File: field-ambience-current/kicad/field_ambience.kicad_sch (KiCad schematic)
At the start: 0 parts

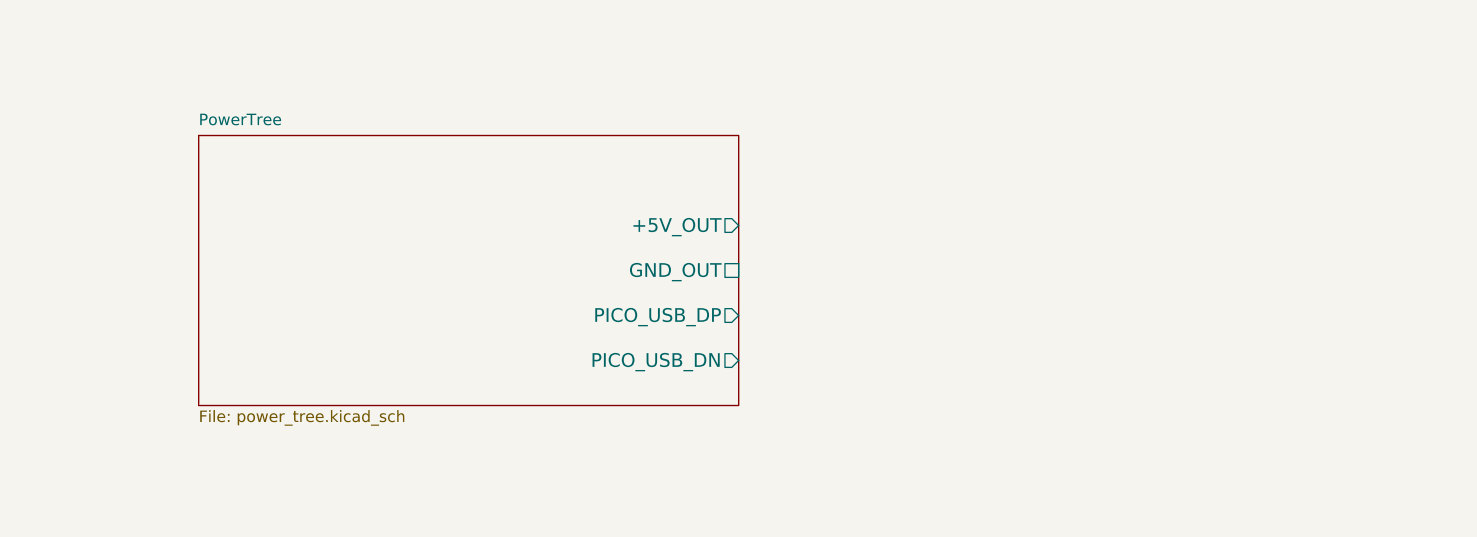
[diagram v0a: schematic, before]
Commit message: Add Sheet 2 (Pico 2) + fix Y-axis convention bug in Sheet 1
CRITICAL FIX in Sheet 1: lib_symbol pins use Y-UP (math) convention,
but schematic placement uses Y-DOWN (screen). Conversion is
abs_pin_y = sym_y - local_pin_y. The original Sheet 1 had USB-C
VBUS pins (A1/A4/B1/B4) actually wired to the GND trunk and GND
pins (A12/A9/B9/B12) wired to the +5V trunk — a power short if built.

Both sheets now use Y-DOWN coords throughout with explicit pin position
constants. The analyzer confirms correct pin_nets assignment:
- J1 (USB-C): VBUS pins → +5V_USB ✓, GND pins → GND ✓
- U1 (Pico 2): all 40 pins map to correct signals per SPEC v0.6 §5

Sheet 2 contents per SPEC v0.6 §5:
- U1 Raspberry Pi Pico 2 (40-pin module)
- All 22 functional GP pins routed to hierarchical outputs to Sheets 3-6
- C3 10µF + C4 100nF +3V3 decoupling near Pico pin 36
- SW11 Reset (6mm tactile) on RUN line with R_RUN pull-up
- SW12 BOOTSEL (DNP for THT-Pico variant)
- LED1 status LED with R19 820Ω current limit on GP26
- J4 3-pin SWD header (SWCLK/GND/SWDIO) for picoprobe debugging
- 8× GND power symbols on all Pico GND pins

Root sheet now contains both PowerTree + Pico sheets with inter-sheet
wires for +5V, USB_DP, USB_DN.

Analyzer status: 0 errors, 35 warnings (down from 39 before fix).
Remaining warnings are non-blocking: missing datasheets/ dir, NT-001
single-pin nets on hierarchical labels that will close in Sheets 3-7.
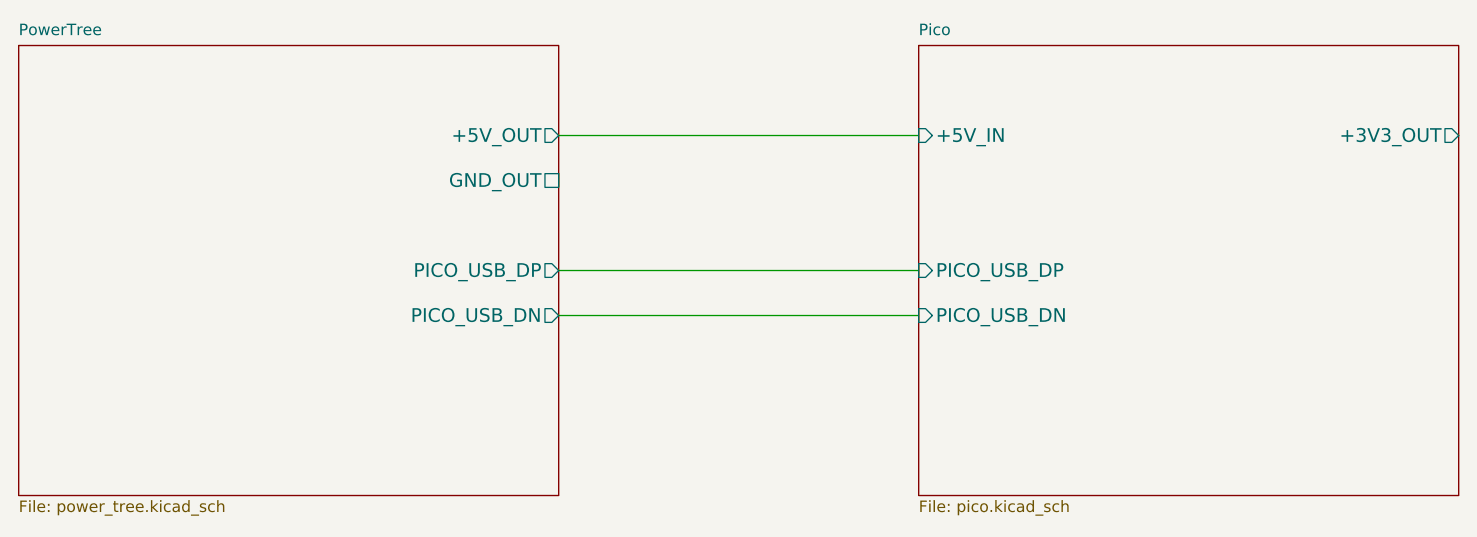
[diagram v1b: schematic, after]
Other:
- added sheet Pico (pico.kicad_sch)
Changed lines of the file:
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@@
     (rev "0.6")
     (company "Field Ambience Project"))
-  (sheet (at 50 50) (size 60 30) (fields_autoplaced)
+  (sheet (at 30 40) (size 60 50) (fields_autoplaced)
     (stroke (width 0.1524) (type solid))
     (fill (color 0 0 0 0.0000))
-    (property "Sheetname" "PowerTree" (at 50 49 0)
+    (property "Sheetname" "PowerTree" (at 30 39 0)
       (effects (font (size 1.27 1.27)) (justify left bottom)))
-    (property "Sheetfile" "power_tree.kicad_sch" (at 50 80.5 0)
+    (property "Sheetfile" "power_tree.kicad_sch" (at 30 90.5 0)
       (effects (font (size 1.27 1.27)) (justify left top)))
-    (pin "+5V_OUT" output (at 110 60 0)
+    (pin "+5V_OUT" output (at 90 50 0)
       (effects (font (size 1.524 1.524)) (justify right))
 )
-    (pin "GND_OUT" passive (at 110 65 0)
+    (pin "GND_OUT" passive (at 90 55 0)
       (effects (font (size 1.524 1.524)) (justify right))
 )
-    (pin "PICO_USB_DP" output (at 110 70 0)
+    (pin "PICO_USB_DP" output (at 90 65 0)
       (effects (font (size 1.524 1.524)) (justify right))
 )
-    (pin "PICO_USB_DN" output (at 110 75 0)
+    (pin "PICO_USB_DN" output (at 90 70 0)
       (effects (font (size 1.524 1.524)) (justify right))
 ))
+  (sheet (at 130 40) (size 60 50) (fields_autoplaced)
+    (stroke (width 0.1524) (type solid))
+    (fill (color 0 0 0 0.0000))
+    (property "Sheetname" "Pico" (at 130 39 0)
+      (effects (font (size 1.27 1.27)) (justify left bottom)))
+    (property "Sheetfile" "pico.kicad_sch" (at 130 90.5 0)
+      (effects (font (size 1.27 1.27)) (justify left top)))
+    (pin "+5V_IN" input (at 130 50 180)
+      (effects (font (size 1.524 1.524)) (justify left))
+)
+    (pin "PICO_USB_DP" input (at 130 65 180)
+      (effects (font (size 1.524 1.524)) (justify left))
+)
+    (pin "PICO_USB_DN" input (at 130 70 180)
+      (effects (font (size 1.524 1.524)) (justify left))
+)
+    (pin "+3V3_OUT" output (at 190 50 0)
+      (effects (font (size 1.524 1.524)) (justify right))
+))
+  (wire (pts (xy 90 50) (xy 130 50)) (stroke (width 0) (type default)))
+  (wire (pts (xy 90 65) (xy 130 65)) (stroke (width 0) (type default)))
+  (wire (pts (xy 90 70) (xy 130 70)) (stroke (width 0) (type default)))
   (sheet_instances
     (path "/" (page "1")))

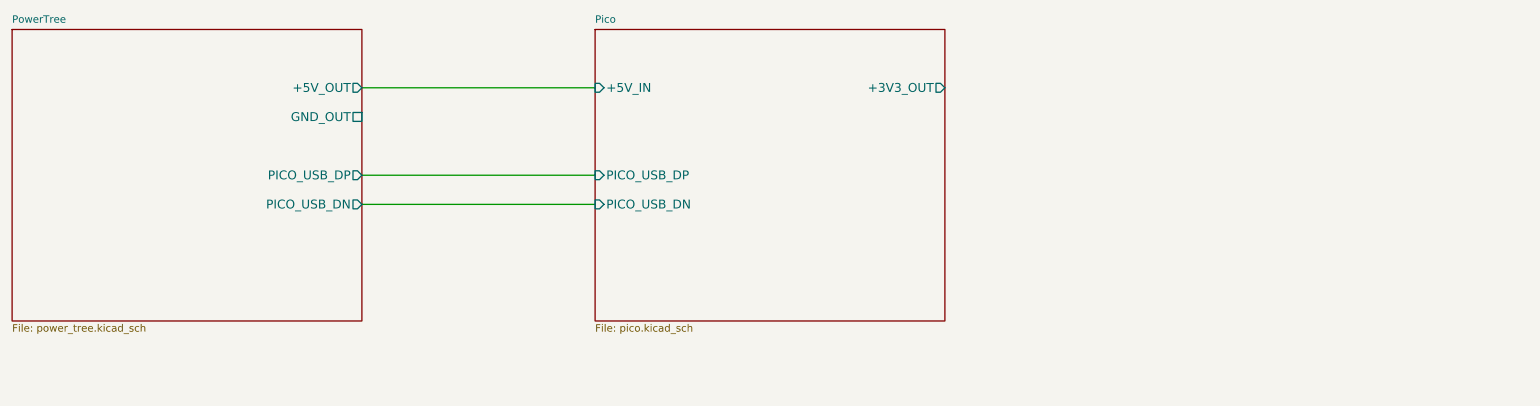
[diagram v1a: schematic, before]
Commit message: Add Sheet 3 (OLED) per SPEC v0.6 §6
J3 16-pin header für ER-OLEDM032-1W 256x64 SSD1322 OLED-Modul:
- Pin 1 VSS → GND
- Pin 2 VBAT → +5V mit lokalem C6b 10µF + C6c 100nF (250mA peak)
- Pin 3 VDD → +3V3 mit lokalem C6 100nF (Logic)
- Pin 4, 14-16 NC (Labels gegen Dangling-Wire-Warnings)
- Pin 5 BS1, Pin 6 BS0 → GND (4-wire SPI mode)
- Pin 7 RES#, Pin 8 CS#, Pin 9 DC# → OLED_RES/CS/DC (Pico GP9/5/8)
- Pin 10 E/RW, Pin 11 RW/E → GND (4-wire SPI unused)
- Pin 12 SCLK, Pin 13 SDIN → OLED_SCK/MOSI (Pico GP6/7)

Root sheet erweitert mit OLED sheet pin + inter-sheet SPI bus wires
zwischen Pico und OLED (SCK/MOSI/CS/DC/RES).

Generic Conn_01x16 lib_symbol generator added.

Analyzer: 0 errors, 30 warnings (down from 35), 20 components total.
All J3 pin_nets verified correct via analyzer pin_nets dump.
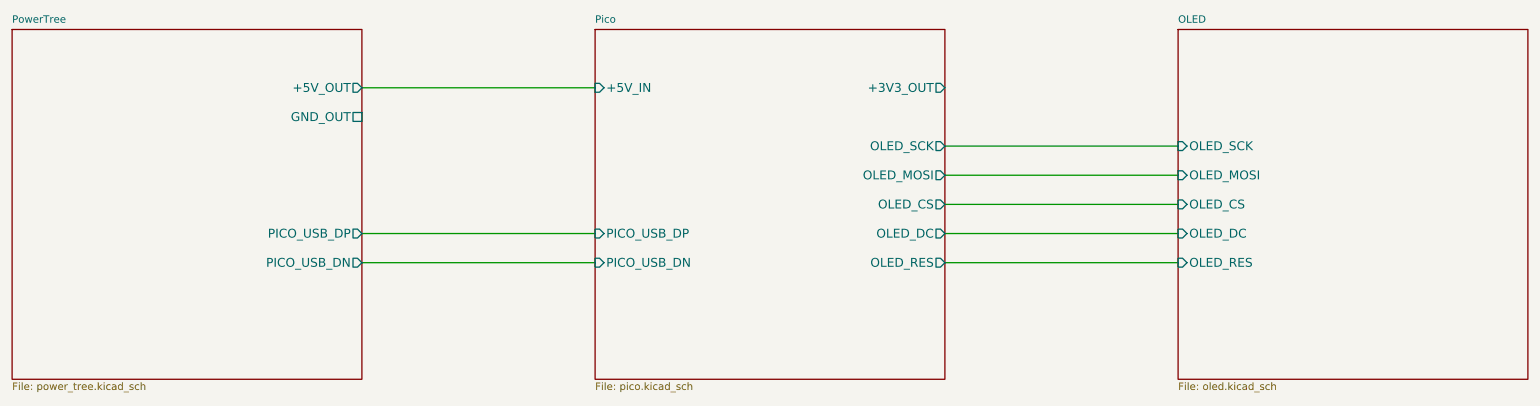
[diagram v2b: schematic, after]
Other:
- added sheet OLED (oled.kicad_sch)
- sheet Pico ports: added OLED_CS, OLED_DC, OLED_MOSI, OLED_RES, OLED_SCK; removed none
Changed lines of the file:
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@@
   (title_block
     (title "Field Ambience PCB — Root")
-    (date "2026-05-11")
+    (date "2026-05-12")
     (rev "0.6")
     (company "Field Ambience Project"))
-  (sheet (at 30 40) (size 60 50) (fields_autoplaced)
+  (sheet (at 30 40) (size 60 60) (fields_autoplaced)
     (stroke (width 0.1524) (type solid))
     (fill (color 0 0 0 0.0000))
     (property "Sheetname" "PowerTree" (at 30 39 0)
       (effects (font (size 1.27 1.27)) (justify left bottom)))
-    (property "Sheetfile" "power_tree.kicad_sch" (at 30 90.5 0)
+    (property "Sheetfile" "power_tree.kicad_sch" (at 30 100.5 0)
       (effects (font (size 1.27 1.27)) (justify left top)))
     (pin "+5V_OUT" output (at 90 50 0)
@@
       (effects (font (size 1.524 1.524)) (justify right))
 )
-    (pin "PICO_USB_DP" output (at 90 65 0)
+    (pin "PICO_USB_DP" output (at 90 75 0)
       (effects (font (size 1.524 1.524)) (justify right))
 )
-    (pin "PICO_USB_DN" output (at 90 70 0)
+    (pin "PICO_USB_DN" output (at 90 80 0)
       (effects (font (size 1.524 1.524)) (justify right))
 ))
-  (sheet (at 130 40) (size 60 50) (fields_autoplaced)
+  (sheet (at 130 40) (size 60 60) (fields_autoplaced)
     (stroke (width 0.1524) (type solid))
     (fill (color 0 0 0 0.0000))
     (property "Sheetname" "Pico" (at 130 39 0)
       (effects (font (size 1.27 1.27)) (justify left bottom)))
-    (property "Sheetfile" "pico.kicad_sch" (at 130 90.5 0)
+    (property "Sheetfile" "pico.kicad_sch" (at 130 100.5 0)
       (effects (font (size 1.27 1.27)) (justify left top)))
     (pin "+5V_IN" input (at 130 50 180)
       (effects (font (size 1.524 1.524)) (justify left))
 )
-    (pin "PICO_USB_DP" input (at 130 65 180)
+    (pin "PICO_USB_DP" input (at 130 75 180)
       (effects (font (size 1.524 1.524)) (justify left))
 )
-    (pin "PICO_USB_DN" input (at 130 70 180)
+    (pin "PICO_USB_DN" input (at 130 80 180)
       (effects (font (size 1.524 1.524)) (justify left))
 )
     (pin "+3V3_OUT" output (at 190 50 0)
       (effects (font (size 1.524 1.524)) (justify right))
+)
+    (pin "OLED_SCK" output (at 190 60 0)
+      (effects (font (size 1.524 1.524)) (justify right))
+)
+    (pin "OLED_MOSI" output (at 190 65 0)
+      (effects (font (size 1.524 1.524)) (justify right))
+)
+    (pin "OLED_CS" output (at 190 70 0)
+      (effects (font (size 1.524 1.524)) (justify right))
+)
+    (pin "OLED_DC" output (at 190 75 0)
+      (effects (font (size 1.524 1.524)) (justify right))
+)
+    (pin "OLED_RES" output (at 190 80 0)
+      (effects (font (size 1.524 1.524)) (justify right))
+))
+  (sheet (at 230 40) (size 60 60) (fields_autoplaced)
+    (stroke (width 0.1524) (type solid))
+    (fill (color 0 0 0 0.0000))
+    (property "Sheetname" "OLED" (at 230 39 0)
+      (effects (font (size 1.27 1.27)) (justify left bottom)))
+    (property "Sheetfile" "oled.kicad_sch" (at 230 100.5 0)
+      (effects (font (size 1.27 1.27)) (justify left top)))
+    (pin "OLED_SCK" input (at 230 60 180)
+      (effects (font (size 1.524 1.524)) (justify left))
+)
+    (pin "OLED_MOSI" input (at 230 65 180)
+      (effects (font (size 1.524 1.524)) (justify left))
+)
+    (pin "OLED_CS" input (at 230 70 180)
+      (effects (font (size 1.524 1.524)) (justify left))
+)
+    (pin "OLED_DC" input (at 230 75 180)
+      (effects (font (size 1.524 1.524)) (justify left))
+)
+    (pin "OLED_RES" input (at 230 80 180)
+      (effects (font (size 1.524 1.524)) (justify left))
 ))
   (wire (pts (xy 90 50) (xy 130 50)) (stroke (width 0) (type default)))
-  (wire (pts (xy 90 65) (xy 130 65)) (stroke (width 0) (type default)))
-  (wire (pts (xy 90 70) (xy 130 70)) (stroke (width 0) (type default)))
+  (wire (pts (xy 90 75) (xy 130 75)) (stroke (width 0) (type default)))
+  (wire (pts (xy 90 80) (xy 130 80)) (stroke (width 0) (type default)))
+  (wire (pts (xy 190 60) (xy 230 60)) (stroke (width 0) (type default)))
+  (wire (pts (xy 190 65) (xy 230 65)) (stroke (width 0) (type default)))
+  (wire (pts (xy 190 70) (xy 230 70)) (stroke (width 0) (type default)))
+  (wire (pts (xy 190 75) (xy 230 75)) (stroke (width 0) (type default)))
+  (wire (pts (xy 190 80) (xy 230 80)) (stroke (width 0) (type default)))
   (sheet_instances
     (path "/" (page "1")))

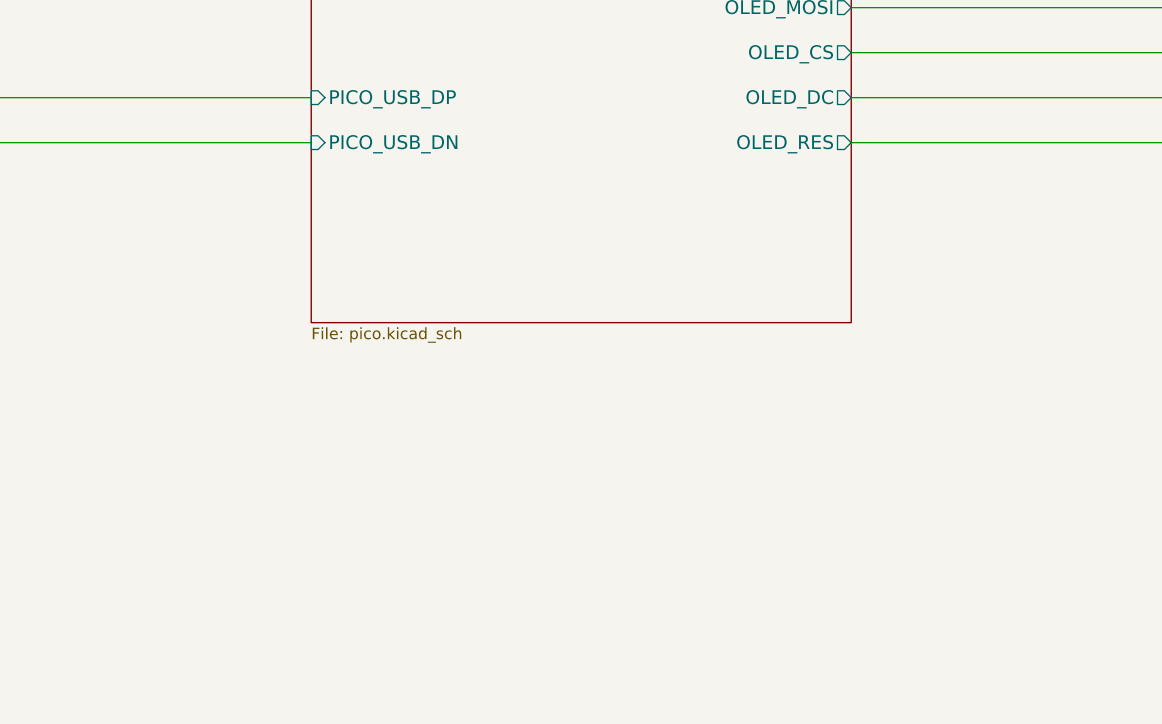
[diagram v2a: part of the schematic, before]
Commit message: Add Sheet 4 (MCP23017 + 10 Switches) per SPEC v0.6 §7
U2 MCP23017-E/SS (SSOP-28, C506653) als I/O-Expander mit:
- I²C-Adresse 0x20 (A0=A1=A2=GND, Pin 15/16/17)
- Pin 12 SCL, Pin 13 SDA → Pico GP3/GP2 via Hier-Labels
- R4 4.7k SDA Pull-Up, R5 4.7k SCL Pull-Up zu +3V3
- Pin 9 VDD → +3V3 mit C5 100nF + C5b 10nF Decoupling
- Pin 10 VSS → GND
- Pin 18 ~RESET → R6 10k Pull-Up zu +3V3
- Pin 20 INTA → R20 10k Pull-Up zu +3V3 (SPEC v0.6 H3-Fix)
  + Hier-Output MCP_INT zu Pico GP22
- Pin 19 INTB → NC (MIRROR=1 in IOCON Firmware-config)

10 Switches Kailh Choc V2 Hot-Swap (user-supplied, JLC stockt nicht):
- SW1-SW5 (Cells, 2u): GPA0-GPA4 → CELL1-CELL5
- SW6-SW10 (Modifier, 1u): GPB0-GPB4 → MOD_SHIFT/HOLD/DRONE/GENERATE/CLEAR
- Internal Pull-Ups via MCP GPPU register (Firmware)
- Reserve-Pins GPA5-7, GPB5-7 als NC-Labels markiert

Root sheet erweitert: Pico-Sheet exportiert jetzt I2C_SDA, I2C_SCL, MCP_INT;
neuer MCP-Sheet bei (130, 110); Cross-Sheet via Labels statt Wires (da
räumlich versetzt zwischen oberen Pico und unteren MCP Sheet-Boxen).

Analyzer-Status: 0 functional errors, 3 VM-001 false-positives (analyzer
schätzt Pico als 5V-Domain wegen VBUS-Pin, obwohl GPIO 3V3 sind — kein
echtes Domain-Crossing; alle I2C+INT-Signale sind 3V3-only).

Total components: 37, 98 nets. Korrekte Pin-Allocation verifiziert via
analyzer.pin_nets-Dump für U2 alle 28 Pins.
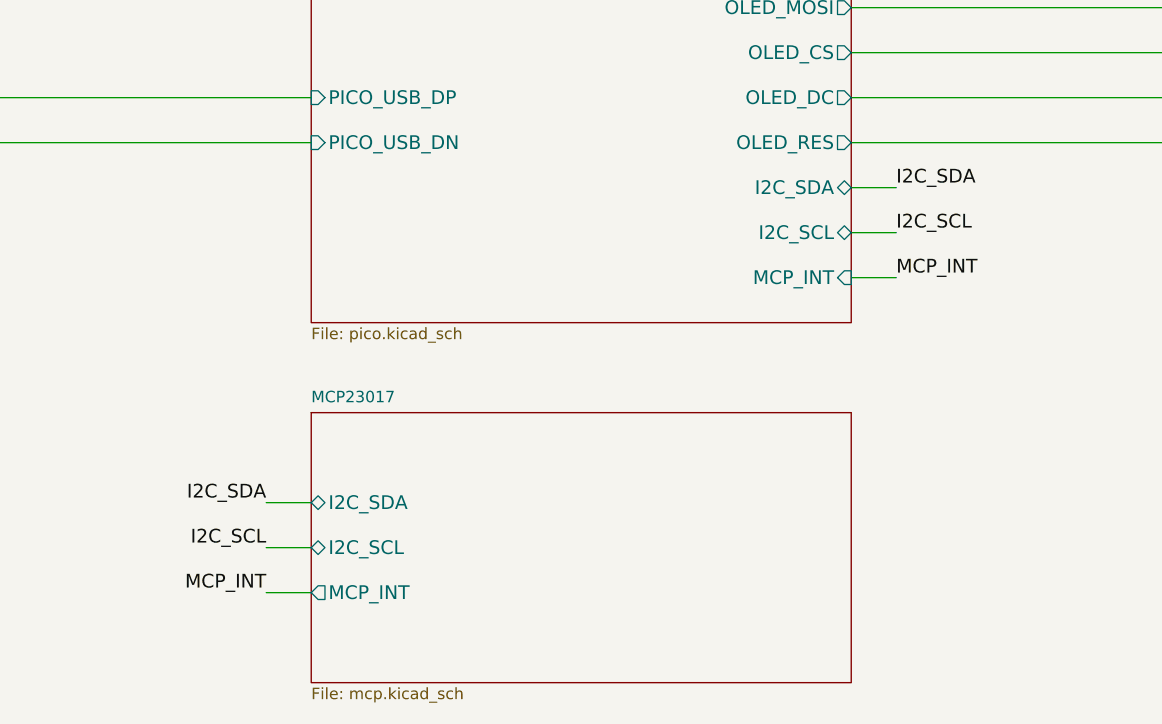
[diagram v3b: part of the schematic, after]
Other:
- added sheet MCP23017 (mcp.kicad_sch)
- sheet Pico ports: added I2C_SCL, I2C_SDA, MCP_INT; removed none
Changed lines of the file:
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@@
     (pin "OLED_RES" output (at 190 80 0)
+      (effects (font (size 1.524 1.524)) (justify right))
+)
+    (pin "I2C_SDA" bidirectional (at 190 85 0)
+      (effects (font (size 1.524 1.524)) (justify right))
+)
+    (pin "I2C_SCL" bidirectional (at 190 90 0)
+      (effects (font (size 1.524 1.524)) (justify right))
+)
+    (pin "MCP_INT" input (at 190 95 0)
       (effects (font (size 1.524 1.524)) (justify right))
 ))
@@
       (effects (font (size 1.524 1.524)) (justify left))
 ))
+  (sheet (at 130 110) (size 60 30) (fields_autoplaced)
+    (stroke (width 0.1524) (type solid))
+    (fill (color 0 0 0 0.0000))
+    (property "Sheetname" "MCP23017" (at 130 109 0)
+      (effects (font (size 1.27 1.27)) (justify left bottom)))
+    (property "Sheetfile" "mcp.kicad_sch" (at 130 140.5 0)
+      (effects (font (size 1.27 1.27)) (justify left top)))
+    (pin "I2C_SDA" bidirectional (at 130 120 180)
+      (effects (font (size 1.524 1.524)) (justify left))
+)
+    (pin "I2C_SCL" bidirectional (at 130 125 180)
+      (effects (font (size 1.524 1.524)) (justify left))
+)
+    (pin "MCP_INT" output (at 130 130 180)
+      (effects (font (size 1.524 1.524)) (justify left))
+))
   (wire (pts (xy 90 50) (xy 130 50)) (stroke (width 0) (type default)))
   (wire (pts (xy 90 75) (xy 130 75)) (stroke (width 0) (type default)))
@@
   (wire (pts (xy 190 75) (xy 230 75)) (stroke (width 0) (type default)))
   (wire (pts (xy 190 80) (xy 230 80)) (stroke (width 0) (type default)))
+  (wire (pts (xy 190 85) (xy 195 85)) (stroke (width 0) (type default)))
+  (label "I2C_SDA" (at 195 85 0) (effects (font (size 1.524 1.524)) (justify left bottom)))
+  (wire (pts (xy 190 90) (xy 195 90)) (stroke (width 0) (type default)))
+  (label "I2C_SCL" (at 195 90 0) (effects (font (size 1.524 1.524)) (justify left bottom)))
+  (wire (pts (xy 190 95) (xy 195 95)) (stroke (width 0) (type default)))
+  (label "MCP_INT" (at 195 95 0) (effects (font (size 1.524 1.524)) (justify left bottom)))
+  (wire (pts (xy 125 120) (xy 130 120)) (stroke (width 0) (type default)))
+  (label "I2C_SDA" (at 125 120 0) (effects (font (size 1.524 1.524)) (justify right bottom)))
+  (wire (pts (xy 125 125) (xy 130 125)) (stroke (width 0) (type default)))
+  (label "I2C_SCL" (at 125 125 0) (effects (font (size 1.524 1.524)) (justify right bottom)))
+  (wire (pts (xy 125 130) (xy 130 130)) (stroke (width 0) (type default)))
+  (label "MCP_INT" (at 125 130 0) (effects (font (size 1.524 1.524)) (justify right bottom)))
   (sheet_instances
     (path "/" (page "1")))
